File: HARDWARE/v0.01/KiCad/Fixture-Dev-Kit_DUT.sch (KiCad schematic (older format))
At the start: 33 parts, among them J62 Conn_01x20, J63 Conn_01x20, J64 Conn_01x20, J65 Conn_01x20, J66 CHIP4RH, J67 CHIP4LH, J68 Conn_01x35, J69 CHIP4B2B, J70 VBUS, J71 A_D+, J72 USB_OTG, J73 B_D-, J74 USB_A, J75 B_D+, J76 A_D-, J77 USB_ID, J78 Conn_01x35, J79 BAT, J80 UPDATE, J81 D-TP's, J82 ANT--SELECT, SW10 SW_Push

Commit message: updating the cover page
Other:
- note added: "DUT - B2B Conn"
- note added: "DUT - Left Header"
- note added: "DUT - Right Header"
- moved on the sheet: J62, J63, J64, J65, J66, J67, J68, J69, J78

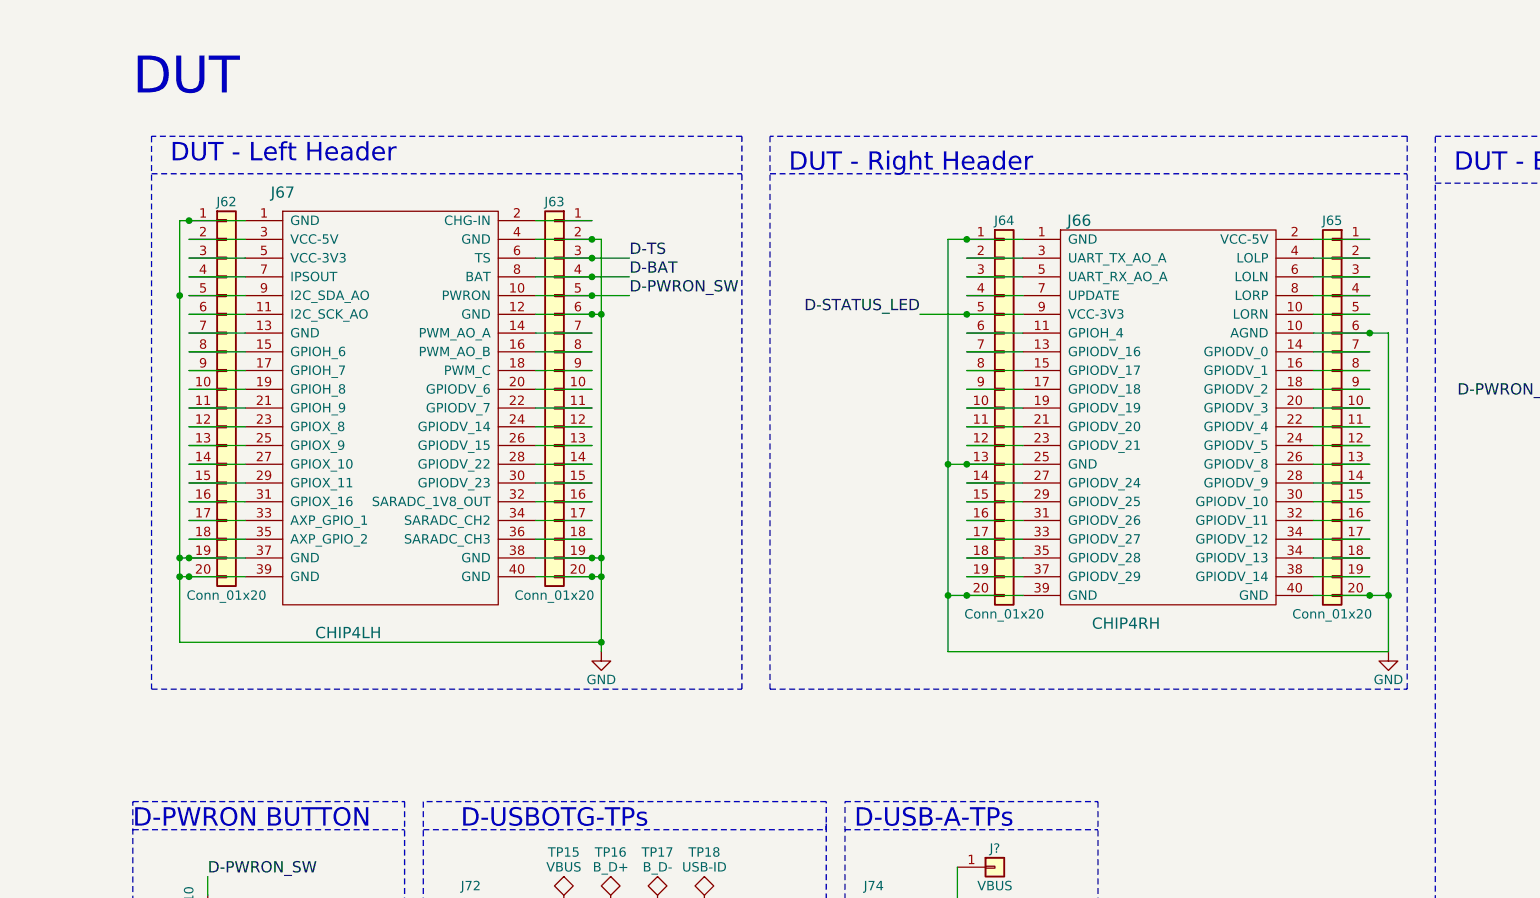
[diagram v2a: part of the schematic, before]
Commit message: adding labelings, hierarchy pins, and page titles
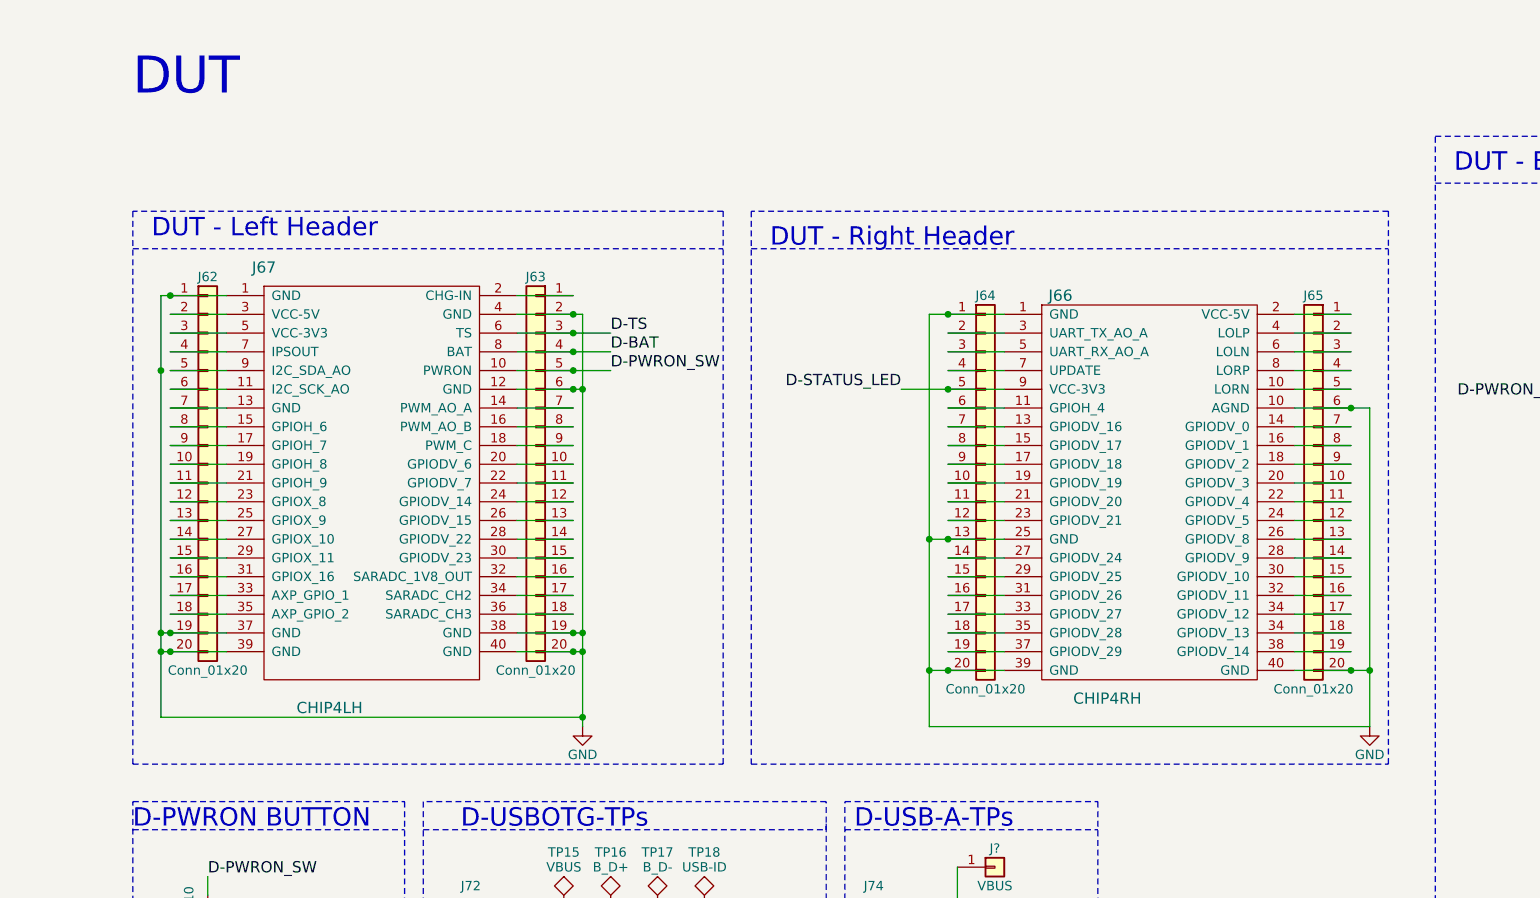
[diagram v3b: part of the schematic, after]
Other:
- moved on the sheet: J62, J63, J64, J65, J66, J67

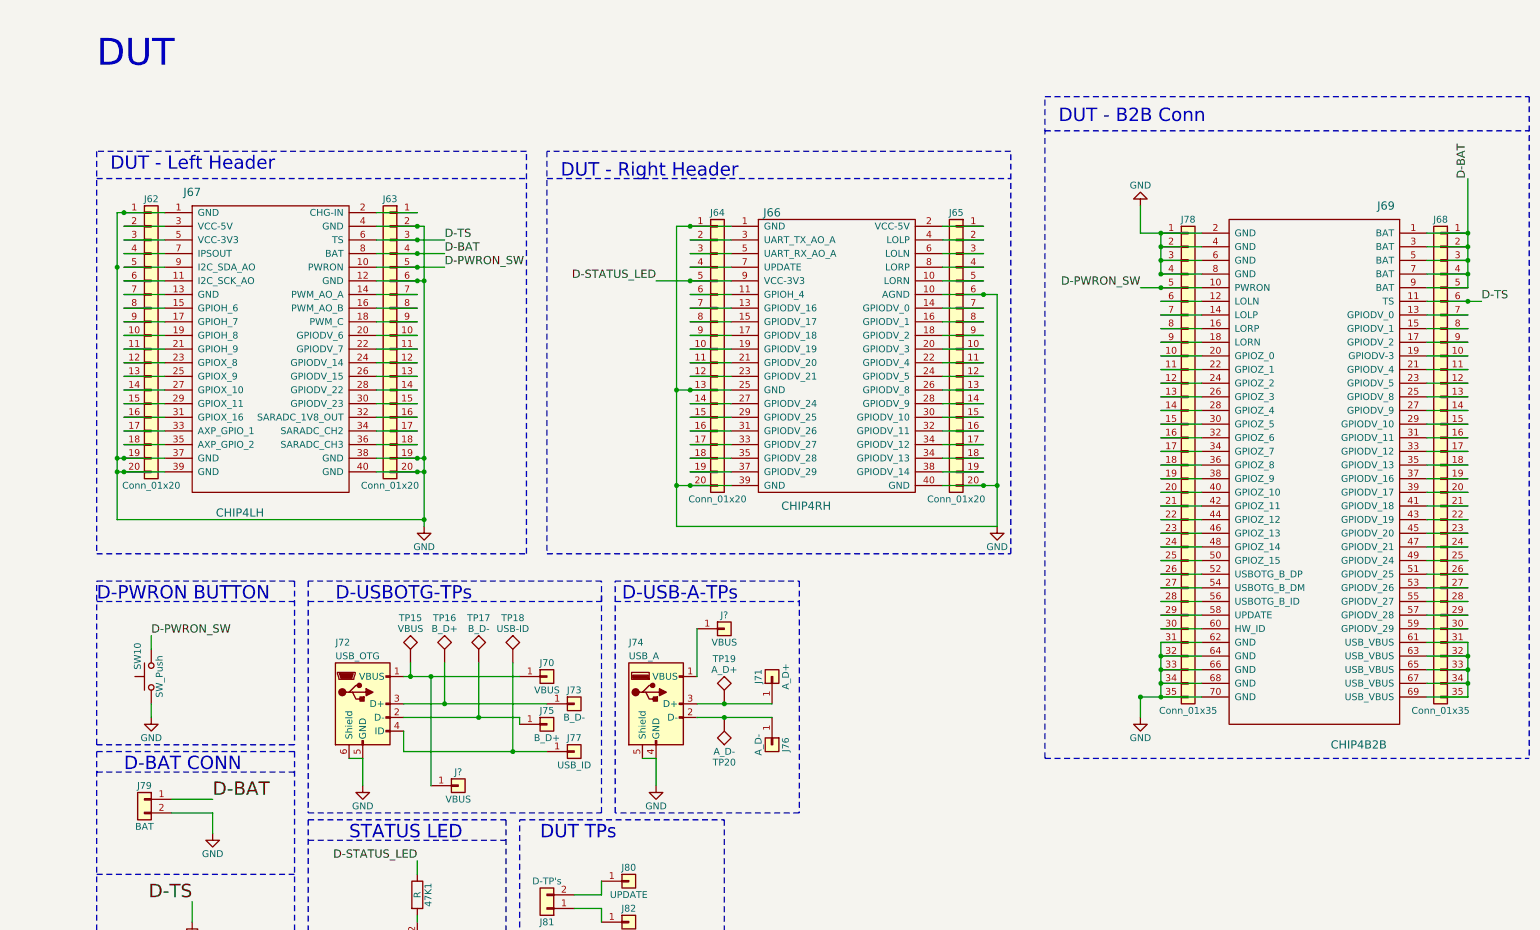
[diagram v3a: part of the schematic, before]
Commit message: adjusting page sizes and cleaning up schematics
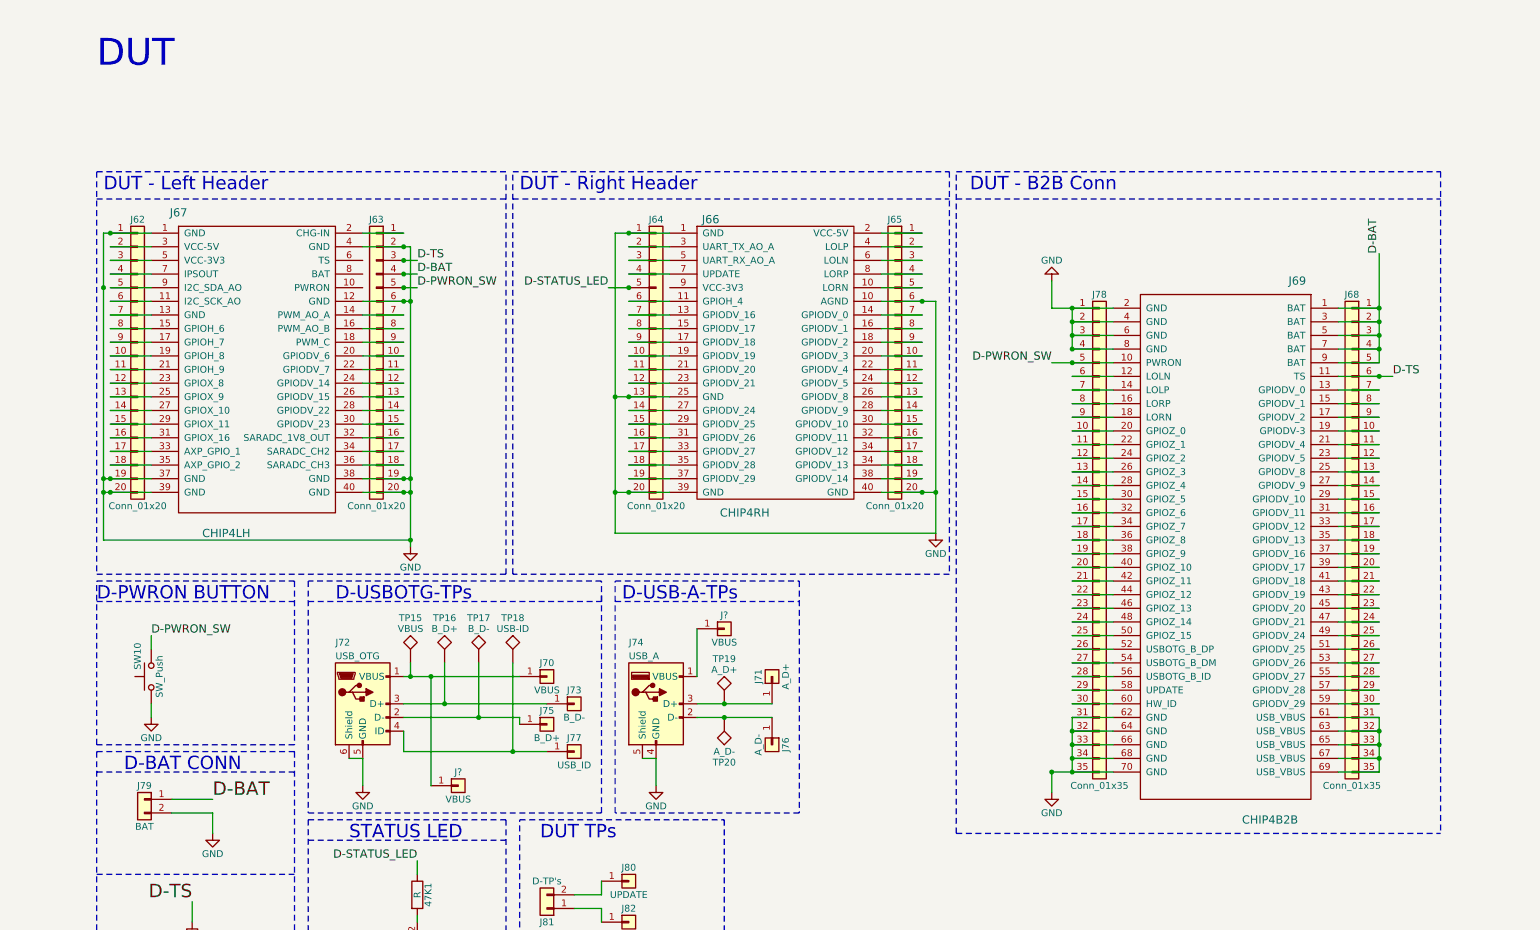
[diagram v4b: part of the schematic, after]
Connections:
- net D-BAT: no longer J67.8 (BAT)
- net D-PWRON_SW: no longer J67.10 (PWRON)
- net D-STATUS_LED: no longer J66.9 (VCC-3V3)
- net D-TS: no longer J67.6 (TS)
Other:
- moved on the sheet: J62, J63, J64, J65, J66, J67, J68, J69, J78

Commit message: cleaning up schematic, run rules check, generate net list
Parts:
- gave numbers to parts that had none: 2
- renumbered D11 to D13, J62 to J34, J79 to J35, J67 to J36, J72 to J37, J63 to J38, J70 to J40, J75 to J41, J81 to J42, J73 to J43, J77 to J44, J80 to J45, J82 to J46, J64 to J47, J74 to J48, J71 to J50, J76 to J51, J66 to J52, J65 to J53, J78 to J54, J69 to J55, J68 to J56, R63 to R49, SW10 to SW9, TP15 to TP25, TP16 to TP26, TP17 to TP27, TP18 to TP28, TP19 to TP29, TP20 to TP30
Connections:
- net D-BAT: now also J36.8 (BAT)
- net D-PWRON_SW: now also J36.10 (PWRON)
- net D-STATUS_LED: now also J52.9 (VCC-3V3)
- net D-TS: now also J36.6 (TS)

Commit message: adding footprints
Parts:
- J34, J47, J53: footprint (none) -> Pin_Headers:Pin_Header_Straight_1x20_Pitch2.54mm
- J35: footprint (none) -> Connectors_JST:JST_PH_S2B-PH-K_02x2.00mm_Angled
- J36: footprint (none) -> Pin_Headers:Pin_Header_Angled_2x20_Pitch2.54mm
- J38: footprint (none) -> Pin_Headers:Pin_Header_Angled_1x20_Pitch2.54mm
- J39, J40, J41, J43, J44, J45, J46, J49, J50, J51: footprint (none) -> Pin_Headers:Pin_Header_Angled_1x01_Pitch2.54mm
- J42: footprint (none) -> Pin_Headers:Pin_Header_Straight_1x02_Pitch2.54mm
- J54, J56: footprint (none) -> Pin_Headers:Pin_Header_Straight_1x35_Pitch2.54mm
- R49: footprint (none) -> Resistors_SMD:R_0805_HandSoldering
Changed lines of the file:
@@
 F 0 "J53" H 6400 3900 50  0000 C CNN
 F 1 "Conn_01x20" H 6400 1800 50  0000 C CNN
-F 2 "" H 6400 2900 50  0001 C CNN
+F 2 "Pin_Headers:Pin_Header_Straight_1x20_Pitch2.54mm" H 6400 2900 50  0001 C CNN
 F 3 "" H 6400 2900 50  0001 C CNN
 	1    6400 2900
@@
 F 0 "J47" H 4650 3900 50  0000 C CNN
 F 1 "Conn_01x20" H 4650 1800 50  0000 C CNN
-F 2 "" H 4650 2900 50  0001 C CNN
+F 2 "Pin_Headers:Pin_Header_Straight_1x20_Pitch2.54mm" H 4650 2900 50  0001 C CNN
 F 3 "" H 4650 2900 50  0001 C CNN
 	1    4650 2900
@@
 F 0 "J38" H 2600 3900 50  0000 C CNN
 F 1 "Conn_01x20" H 2600 1800 50  0000 C CNN
-F 2 "" H 2600 2900 50  0001 C CNN
+F 2 "Pin_Headers:Pin_Header_Angled_1x20_Pitch2.54mm" H 2600 2900 50  0001 C CNN
 F 3 "" H 2600 2900 50  0001 C CNN
 	1    2600 2900
@@
 F 0 "J34" H 850 3900 50  0000 C CNN
 F 1 "Conn_01x20" H 850 1800 50  0000 C CNN
-F 2 "" H 850 2900 50  0001 C CNN
+F 2 "Pin_Headers:Pin_Header_Straight_1x20_Pitch2.54mm" H 850 2900 50  0001 C CNN
 F 3 "" H 850 2900 50  0001 C CNN
 	1    850  2900
@@
 F 0 "J35" H 900 6250 50  0000 C CNN
 F 1 "BAT" H 900 5950 50  0000 C CNN
-F 2 "" H 900 6150 50  0001 C CNN
+F 2 "Connectors_JST:JST_PH_S2B-PH-K_02x2.00mm_Angled" H 900 6150 50  0001 C CNN
 F 3 "" H 900 6150 50  0001 C CNN
 	1    900  6150
@@
 F 0 "J54" H 7900 6050 50  0000 C CNN
 F 1 "Conn_01x35" H 7900 2450 50  0000 C CNN
-F 2 "" H 7900 4250 50  0001 C CNN
+F 2 "Pin_Headers:Pin_Header_Straight_1x35_Pitch2.54mm" H 7900 4250 50  0001 C CNN
 F 3 "" H 7900 4250 50  0001 C CNN
 	1    7900 4250
@@
 F 0 "J56" H 9750 6050 50  0000 C CNN
 F 1 "Conn_01x35" H 9750 2450 50  0000 C CNN
-F 2 "" H 9750 4250 50  0001 C CNN
+F 2 "Pin_Headers:Pin_Header_Straight_1x35_Pitch2.54mm" H 9750 4250 50  0001 C CNN
 F 3 "" H 9750 4250 50  0001 C CNN
 	1    9750 4250
@@
 F 0 "R49" V 1330 7200 50  0000 C CNN
 F 1 "10K" V 1250 7200 50  0000 C CNN
-F 2 "" V 1180 7200 50  0001 C CNN
+F 2 "Resistors_SMD:R_0805_HandSoldering" V 1180 7200 50  0001 C CNN
 F 3 "" H 1250 7200 50  0001 C CNN
 	1    1250 7200
@@
 F 0 "J36" H 1150 6250 60  0000 C CNN
 F 1 "CHIP4LH" H 1500 3900 60  0000 C CNN
-F 2 "" H 1800 4050 60  0001 C CNN
+F 2 "Pin_Headers:Pin_Header_Angled_2x20_Pitch2.54mm" H 1800 4050 60  0001 C CNN
 F 3 "" H 1800 4050 60  0001 C CNN
 	1    1700 4050
@@
 F 0 "J40" H 3850 5350 50  0000 C CNN
 F 1 "VBUS" H 3850 5150 50  0000 C CNN
-F 2 "" H 3850 5250 50  0001 C CNN
+F 2 "Pin_Headers:Pin_Header_Angled_1x01_Pitch2.54mm" H 3850 5250 50  0001 C CNN
 F 3 "" H 3850 5250 50  0001 C CNN
 	1    3850 5250
@@
 F 0 "J43" H 4050 5550 50  0000 C CNN
 F 1 "B_D-" H 4050 5350 50  0000 C CNN
-F 2 "" H 4050 5450 50  0001 C CNN
+F 2 "Pin_Headers:Pin_Header_Angled_1x01_Pitch2.54mm" H 4050 5450 50  0001 C CNN
 F 3 "" H 4050 5450 50  0001 C CNN
 	1    4050 5450
@@
 F 0 "J41" H 3850 5700 50  0000 C CNN
 F 1 "B_D+" H 3850 5500 50  0000 C CNN
-F 2 "" H 3850 5600 50  0001 C CNN
+F 2 "Pin_Headers:Pin_Header_Angled_1x01_Pitch2.54mm" H 3850 5600 50  0001 C CNN
 F 3 "" H 3850 5600 50  0001 C CNN
 	1    3850 5600
@@
 F 0 "J44" H 4050 5900 50  0000 C CNN
 F 1 "USB_ID" H 4050 5700 50  0000 C CNN
-F 2 "" H 4050 5800 50  0001 C CNN
+F 2 "Pin_Headers:Pin_Header_Angled_1x01_Pitch2.54mm" H 4050 5800 50  0001 C CNN
 F 3 "" H 4050 5800 50  0001 C CNN
 	1    4050 5800
@@
 F 0 "J50" H 5500 5350 50  0000 C CNN
 F 1 "A_D+" H 5500 5150 50  0000 C CNN
-F 2 "" H 5500 5250 50  0001 C CNN
+F 2 "Pin_Headers:Pin_Header_Angled_1x01_Pitch2.54mm" H 5500 5250 50  0001 C CNN
 F 3 "" H 5500 5250 50  0001 C CNN
 	1    5500 5250
@@
 F 0 "J51" H 5500 5850 50  0000 C CNN
 F 1 "A_D-" H 5500 5650 50  0000 C CNN
-F 2 "" H 5500 5750 50  0001 C CNN
+F 2 "Pin_Headers:Pin_Header_Angled_1x01_Pitch2.54mm" H 5500 5750 50  0001 C CNN
 F 3 "" H 5500 5750 50  0001 C CNN
 	1    5500 5750
@@
 F 0 "J45" H 4450 6850 50  0000 C CNN
 F 1 "UPDATE" H 4450 6650 50  0000 C CNN
-F 2 "" H 4450 6750 50  0001 C CNN
+F 2 "Pin_Headers:Pin_Header_Angled_1x01_Pitch2.54mm" H 4450 6750 50  0001 C CNN
 F 3 "" H 4450 6750 50  0001 C CNN
 	1    4450 6750
@@
 F 0 "J46" H 4450 7150 50  0000 C CNN
 F 1 "ANT--SELECT" H 4450 6950 50  0000 C CNN
-F 2 "" H 4450 7050 50  0001 C CNN
+F 2 "Pin_Headers:Pin_Header_Angled_1x01_Pitch2.54mm" H 4450 7050 50  0001 C CNN
 F 3 "" H 4450 7050 50  0001 C CNN
 	1    4450 7050
@@
 F 0 "J42" H 3850 7050 50  0000 C CNN
 F 1 "D-TP's" H 3850 6750 50  0000 C CNN
-F 2 "" H 3850 6950 50  0001 C CNN
+F 2 "Pin_Headers:Pin_Header_Straight_1x02_Pitch2.54mm" H 3850 6950 50  0001 C CNN
 F 3 "" H 3850 6950 50  0001 C CNN
 	1    3850 6950
@@
 F 0 "J39" H 3200 6150 50  0000 C CNN
 F 1 "VBUS" H 3200 5950 50  0000 C CNN
-F 2 "" H 3200 6050 50  0001 C CNN
+F 2 "Pin_Headers:Pin_Header_Angled_1x01_Pitch2.54mm" H 3200 6050 50  0001 C CNN
 F 3 "" H 3200 6050 50  0001 C CNN
 	1    3200 6050
@@
 F 0 "J49" H 5150 5000 50  0000 C CNN
 F 1 "VBUS" H 5150 4800 50  0000 C CNN
-F 2 "" H 5150 4900 50  0001 C CNN
+F 2 "Pin_Headers:Pin_Header_Angled_1x01_Pitch2.54mm" H 5150 4900 50  0001 C CNN
 F 3 "" H 5150 4900 50  0001 C CNN
 	1    5150 4900

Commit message: adding footprints, starting layout
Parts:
- D13: footprint (none) -> LEDs:LED_0805_HandSoldering
- R94: renamed from 47K1; value R -> 47K; footprint (none) -> Resistors_SMD:R_0805_HandSoldering
- TP25, TP26, TP27, TP28, TP29, TP30: footprint (none) -> TestPoint:TestPoint
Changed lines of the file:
@@
 LIBS:contrib
 LIBS:valves
-LIBS:FDN337N
+LIBS:TCA6424ARGJR
 LIBS:Fixture-Dev-Kit-cache
 EELAYER 25 0
@@
 F 0 "D13" H 2900 7300 50  0000 C CNN
 F 1 "LED" H 2900 7100 50  0000 C CNN
-F 2 "" H 2900 7200 50  0001 C CNN
+F 2 "LEDs:LED_0805_HandSoldering" H 2900 7200 50  0001 C CNN
 F 3 "" H 2900 7200 50  0001 C CNN
 	1    2900 7200
@@
 $EndComp
 $Comp
-L R 47K1
+L R R94
 U 1 1 59EEBC3E
 P 2900 6850
-F 0 "47K1" V 2980 6850 50  0000 C CNN
-F 1 "R" V 2900 6850 50  0000 C CNN
-F 2 "" V 2830 6850 50  0001 C CNN
+F 0 "R94" V 2980 6850 50  0000 C CNN
+F 1 "47K" V 2900 6850 50  0000 C CNN
+F 2 "Resistors_SMD:R_0805_HandSoldering" V 2830 6850 50  0001 C CNN
 F 3 "" H 2900 6850 50  0001 C CNN
 	1    2900 6850
@@
 F 0 "TP25" H 2850 5450 50  0000 C BNN
 F 1 "VBUS" H 2850 5400 50  0000 C CNN
-F 2 "" H 2850 5150 50  0001 C CNN
+F 2 "TestPoint:TestPoint" H 2850 5150 50  0001 C CNN
 F 3 "" H 2850 5150 50  0001 C CNN
 	1    2850 5150
@@
 F 0 "TP26" H 3100 5450 50  0000 C BNN
 F 1 "B_D+" H 3100 5400 50  0000 C CNN
-F 2 "" H 3100 5150 50  0001 C CNN
+F 2 "TestPoint:TestPoint" H 3100 5150 50  0001 C CNN
 F 3 "" H 3100 5150 50  0001 C CNN
 	1    3100 5150
@@
 F 0 "TP27" H 3350 5450 50  0000 C BNN
 F 1 "B_D-" H 3350 5400 50  0000 C CNN
-F 2 "" H 3350 5150 50  0001 C CNN
+F 2 "TestPoint:TestPoint" H 3350 5150 50  0001 C CNN
 F 3 "" H 3350 5150 50  0001 C CNN
 	1    3350 5150
@@
 F 0 "TP28" H 3600 5450 50  0000 C BNN
 F 1 "USB-ID" H 3600 5400 50  0000 C CNN
-F 2 "" H 3600 5150 50  0001 C CNN
+F 2 "TestPoint:TestPoint" H 3600 5150 50  0001 C CNN
 F 3 "" H 3600 5150 50  0001 C CNN
 	1    3600 5150
@@
 F 0 "TP30" H 5150 5850 50  0000 C BNN
 F 1 "A_D-" H 5150 5800 50  0000 C CNN
-F 2 "" H 5150 5550 50  0001 C CNN
+F 2 "TestPoint:TestPoint" H 5150 5550 50  0001 C CNN
 F 3 "" H 5150 5550 50  0001 C CNN
 	1    5150 5550
@@
 F 0 "TP29" H 5150 5750 50  0000 C BNN
 F 1 "A_D+" H 5150 5700 50  0000 C CNN
-F 2 "" H 5150 5450 50  0001 C CNN
+F 2 "TestPoint:TestPoint" H 5150 5450 50  0001 C CNN
 F 3 "" H 5150 5450 50  0001 C CNN
 	1    5150 5450

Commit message: updating pcb layout
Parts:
- J38: footprint Pin_Headers:Pin_Header_Angled_1x20_Pitch2.54mm -> Pin_Headers:Pin_Header_Straight_1x20_Pitch2.54mm
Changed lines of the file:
@@
 F 0 "J38" H 2600 3900 50  0000 C CNN
 F 1 "Conn_01x20" H 2600 1800 50  0000 C CNN
-F 2 "Pin_Headers:Pin_Header_Angled_1x20_Pitch2.54mm" H 2600 2900 50  0001 C CNN
+F 2 "Pin_Headers:Pin_Header_Straight_1x20_Pitch2.54mm" H 2600 2900 50  0001 C CNN
 F 3 "" H 2600 2900 50  0001 C CNN
 	1    2600 2900
@@
 	1    0    0    -1
 $EndComp
-Text Notes -1900 -1550 0    197  ~ 0
+Text Notes 13150 2550 0    197  ~ 0
 TO DO:\n- is PWRON and BAT break out necessary if headers \nare already broken out?
 Text Notes 6950 1700 0    98   ~ 0
